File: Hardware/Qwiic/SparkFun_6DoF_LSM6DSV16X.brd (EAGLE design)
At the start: 25.4 x 25.4 mm, 83 parts, among them J1 QWIIC_RIGHT_ANGLE, J2 QWIIC_RIGHT_ANGLE, P1 110pF, P2 110pF, U2 LSM6DSV16X

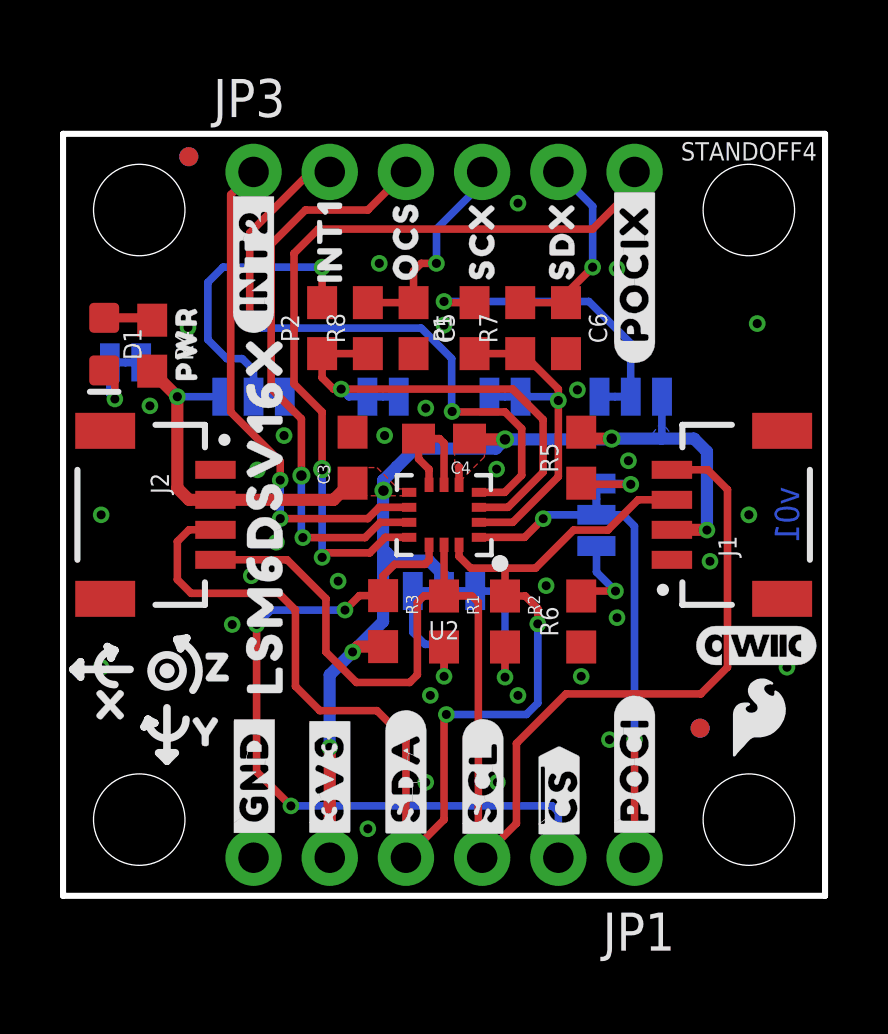
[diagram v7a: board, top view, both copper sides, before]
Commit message: Adds slightly better silk to new three way jumper
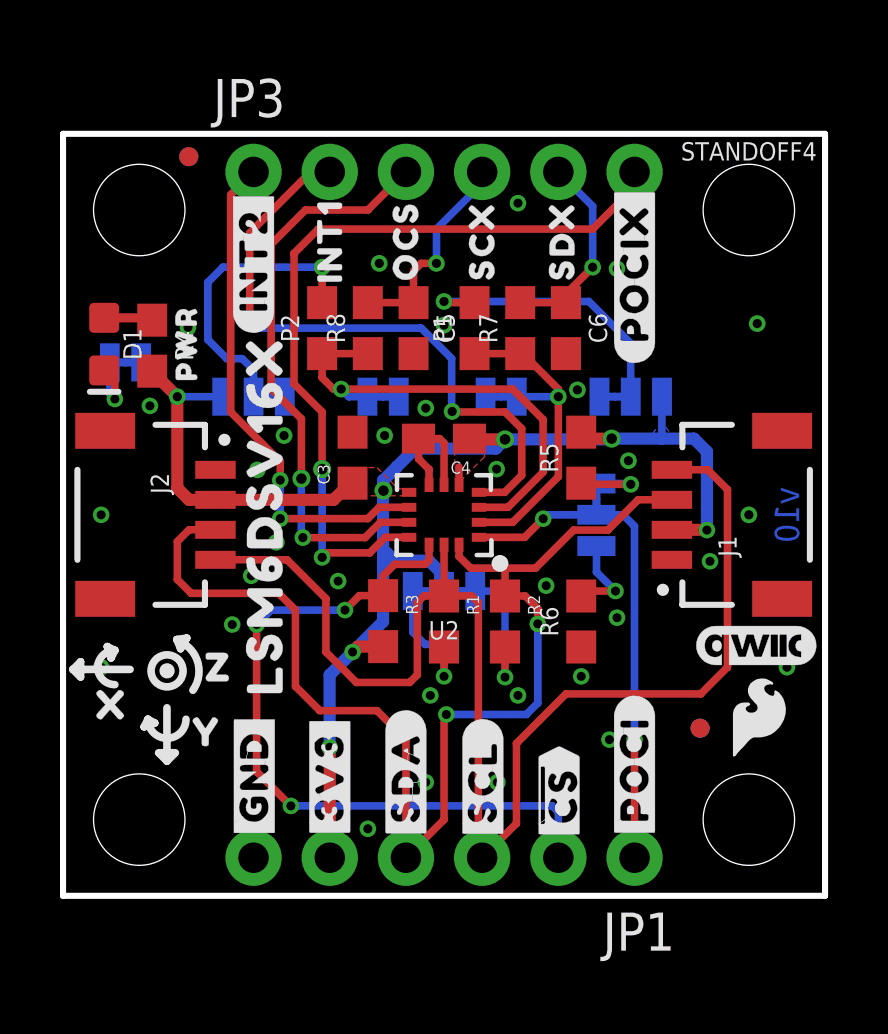
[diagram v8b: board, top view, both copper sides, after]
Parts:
- added U$44: (no value), SparkFun-Aesthetics:SFE_LOGO_FLAME_.2
- added U$45, U$49: (no value), pot:#0#4
- moved U$42 0.13 mm to (14.6, 15.1)
- moved SDX 0.13 mm to (14.6, 16.6)
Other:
- board text added: "v10"
- board text removed: "v01"
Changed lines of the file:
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@@
 <setting verticaltext="up"/>
 </settings>
-<grid distance="0.05" unitdist="inch" unit="inch" style="dots" multiple="1" display="yes" altdistance="0.001" altunitdist="inch" altunit="inch"/>
+<grid distance="0.05" unitdist="inch" unit="inch" style="dots" multiple="1" display="yes" altdistance="0.005" altunitdist="inch" altunit="inch"/>
 <layers>
 <layer number="1" name="Top" color="4" fill="1" visible="yes" active="yes"/>
@@
 <wire x1="0" y1="0" x2="25.4" y2="0" width="0.2032" layer="20"/>
 <wire x1="25.4" y1="0" x2="25.4" y2="25.4" width="0.2032" layer="20"/>
-<text x="24.13" y="12.7" size="0.8128" layer="16" font="vector" ratio="22" rot="SMR270" align="center">v01</text>
+<text x="24.13" y="12.7" size="0.8128" layer="16" font="vector" ratio="22" rot="SMR270" align="center">v10</text>
 <wire x1="0.3302" y1="7.546975" x2="2.2352" y2="7.546975" width="0.254" layer="21"/>
 <wire x1="1.7272" y1="7.038975" x2="1.7272" y2="8.181975" width="0.254" layer="21" curve="-180"/>
@@
 <attribute name="VALUE" x="20.32" y="4.445" size="1.27" layer="27" rot="R180"/>
 </element>
-<element name="SDX" library="SparkFun-Jumpers" package="SMT-JUMPER_2_NC_TRACE_SILK" package3d_urn="urn:adsk.eagle:package:39281/1" value="JUMPER-SMT_2_NC_TRACE_SILK" x="14.732" y="16.637" smashed="yes" rot="MR180">
-<attribute name="NAME" x="13.7795" y="15.367" size="0.4064" layer="26" rot="MR180"/>
-<attribute name="VALUE" x="13.7795" y="18.288" size="0.4064" layer="28" rot="MR180"/>
+<element name="SDX" library="SparkFun-Jumpers" package="SMT-JUMPER_2_NC_TRACE_SILK" package3d_urn="urn:adsk.eagle:package:39281/1" value="JUMPER-SMT_2_NC_TRACE_SILK" x="14.605" y="16.637" smashed="yes" rot="MR180">
+<attribute name="NAME" x="13.6525" y="15.367" size="0.4064" layer="26" rot="MR180"/>
+<attribute name="VALUE" x="13.6525" y="18.288" size="0.4064" layer="28" rot="MR180"/>
 </element>
 <element name="SCX" library="SparkFun-Jumpers" package="SMT-JUMPER_2_NC_TRACE_SILK" package3d_urn="urn:adsk.eagle:package:39281/1" value="JUMPER-SMT_2_NC_TRACE_SILK" x="10.668" y="16.637" smashed="yes" rot="MR0">
@@
 <element name="U$10" library="top" package="SCX18" value="" x="13.97" y="21.844" smashed="yes" rot="R90"/>
 <element name="U$11" library="top" package="SDX19" value="" x="16.637" y="21.844" smashed="yes" rot="R90"/>
-<element name="U$42" library="top" package="#SDX#20" value="" x="14.7066" y="15.1384" smashed="yes" rot="MR0"/>
+<element name="U$42" library="top" package="#SDX#20" value="" x="14.5796" y="15.1384" smashed="yes" rot="MR0"/>
 <element name="U$43" library="top" package="#SCX#19" value="" x="10.6426" y="15.1638" smashed="yes" rot="MR0"/>
 <element name="U$46" library="top" package="LSM6DSV16X37" value="" x="1.3716" y="10.0838" smashed="yes" rot="MR270"/>
@@
 <element name="U$30" library="pot" package="#P2#4" value="" x="6.2484" y="15.0622" smashed="yes" rot="MR0"/>
 <element name="U$32" library="top" package="#1#729" value="" x="21.1582" y="16.637" smashed="yes" rot="MR0"/>
+<element name="U$44" library="SparkFun-Aesthetics" package="SFE_LOGO_FLAME_.2" value="" x="7.62" y="10.16" smashed="yes" rot="MR0"/>
+<element name="U$45" library="pot" package="#0#4" value="" x="8.636" y="16.637" smashed="yes" rot="MR0"/>
+<element name="U$49" library="pot" package="#0#4" value="" x="16.637" y="16.637" smashed="yes" rot="MR180"/>
 </elements>
 <signals>
@@
 <contactref element="U2" pad="P2"/>
 <wire x1="13.8625" y1="12.45" x2="14.99" y2="12.45" width="0.254" layer="1"/>
-<wire x1="16.51" y1="13.97" x2="16.51" y2="16.51" width="0.254" layer="1"/>
-<via x="16.51" y="16.51" extent="1-16" drill="0.3048"/>
-<wire x1="16.51" y1="16.51" x2="16.383" y2="16.637" width="0.254" layer="16"/>
-<wire x1="16.383" y1="16.637" x2="15.2527" y2="16.637" width="0.254" layer="16"/>
+<wire x1="16.51" y1="13.97" x2="16.51" y2="16.637" width="0.254" layer="1"/>
+<via x="16.51" y="16.637" extent="1-16" drill="0.3048"/>
+<wire x1="16.51" y1="16.637" x2="15.1257" y2="16.637" width="0.254" layer="16"/>
 <wire x1="14.99" y1="12.45" x2="16.51" y2="13.97" width="0.254" layer="1"/>
 <contactref element="R7" pad="1"/>
 <contactref element="P1" pad="1"/>
 <wire x1="15.24" y1="18.073" x2="13.716" y2="18.073" width="0.254" layer="1"/>
-<wire x1="16.51" y1="16.51" x2="16.51" y2="16.891" width="0.254" layer="1"/>
+<wire x1="16.51" y1="16.637" x2="16.51" y2="16.891" width="0.254" layer="1"/>
 <wire x1="16.51" y1="16.891" x2="15.328" y2="18.073" width="0.254" layer="1"/>
 <wire x1="15.328" y1="18.073" x2="15.24" y2="18.073" width="0.254" layer="1"/>
@@
 <wire x1="7.239" y1="14.478" x2="5.588" y2="16.129" width="0.254" layer="1"/>
 <wire x1="5.588" y1="23.368" x2="6.35" y2="24.13" width="0.254" layer="1"/>
-<wire x1="5.588" y1="23.368" x2="5.588" y2="16.129" width="0.254" layer="1"/>
+<wire x1="5.588" y1="23.368" x2="5.588" y2="17.78" width="0.254" layer="1"/>
+<wire x1="5.588" y1="17.78" x2="5.588" y2="16.129" width="0.254" layer="1"/>
 </signal>
 <signal name="3.3V">
@@
 <contactref element="PAD1" pad="1"/>
 <contactref element="PAD2" pad="1"/>
-<wire x1="11.1125" y1="14.2875" x2="10.9855" y2="14.1605" width="0.254" layer="16"/>
-<wire x1="5.3086" y1="16.637" x2="3.81" y2="16.636996875" width="0.254" layer="16"/>
 <via x="3.81" y="16.636996875" extent="1-16" drill="0.3048"/>
 <wire x1="19.9644" y1="16.637" x2="19.9644" y2="15.2654" width="0.254" layer="16"/>
@@
 <polygon width="0.127" layer="1" orphans="yes" thermals="no">
 <vertex x="13.0556" y="14.351"/>
-<vertex x="13.0556" y="14.351"/>
 <vertex x="13.0556" y="15.6718"/>
 <vertex x="14.0462" y="15.6718"/>
@@
 </polygon>
 <wire x1="13.2" y1="13.7" x2="13.2" y2="14.2922" width="0.254" layer="1"/>
-<wire x1="13.2" y1="14.2922" x2="13.208" y2="14.3002" width="0.254" layer="1"/>
 <polygon width="0.127" layer="1" orphans="yes" thermals="no">
 <vertex x="11.7348" y="13.335"/>
@@
 <vertex x="11.7348" y="13.5636"/>
 </polygon>
+<wire x1="5.3086" y1="16.637" x2="5.308596875" y2="16.636996875" width="0.254" layer="16"/>
+<wire x1="5.308596875" y1="16.636996875" x2="3.81" y2="16.636996875" width="0.254" layer="16"/>
 </signal>
 <signal name="OCS">
@@
 <via x="7.9929625" y="11.9404" extent="1-16" drill="0.3048"/>
 <wire x1="7.9929625" y1="11.9404" x2="7.945" y2="11.9883625" width="0.254" layer="16"/>
-<wire x1="7.945" y1="11.9883625" x2="7.945" y2="14.00820625" width="0.254" layer="16"/>
-<via x="7.945" y="14.00820625" extent="1-16" drill="0.35"/>
-<wire x1="7.945" y1="14.00820625" x2="7.945" y2="15.90018125" width="0.254" layer="1"/>
+<wire x1="7.945" y1="11.9883625" x2="7.945" y2="13.90660625" width="0.254" layer="16"/>
+<via x="7.945" y="13.90660625" extent="1-16" drill="0.35"/>
+<wire x1="7.945" y1="13.90660625" x2="7.945" y2="15.90018125" width="0.254" layer="1"/>
 <wire x1="7.945" y1="15.90018125" x2="6.937" y2="16.90818125" width="0.254" layer="1"/>
 <wire x1="6.937" y1="16.90818125" x2="6.937" y2="21.717" width="0.254" layer="1"/>
@@
 <wire x1="13.97" y1="23.749" x2="13.97" y2="24.13" width="0.254" layer="16"/>
 <wire x1="12.446" y1="22.225" x2="13.97" y2="23.749" width="0.254" layer="16"/>
-<wire x1="11.684" y1="19.773" x2="11.8305" y2="19.9195" width="0.1524" layer="1"/>
 <wire x1="11.684" y1="19.773" x2="11.684" y2="20.828" width="0.254" layer="1"/>
 <wire x1="11.938" y1="21.082" x2="12.446" y2="21.082" width="0.254" layer="1"/>
